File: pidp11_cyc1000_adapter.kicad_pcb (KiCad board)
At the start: 2 copper layers, 73.7 x 61 mm, 16 parts, among them J1 PIDP11_HDR, J2 USB_B_Micro, J3 PMODNIC100, J4 Conn_01x02, U1 CYC1000, U2 CP2102

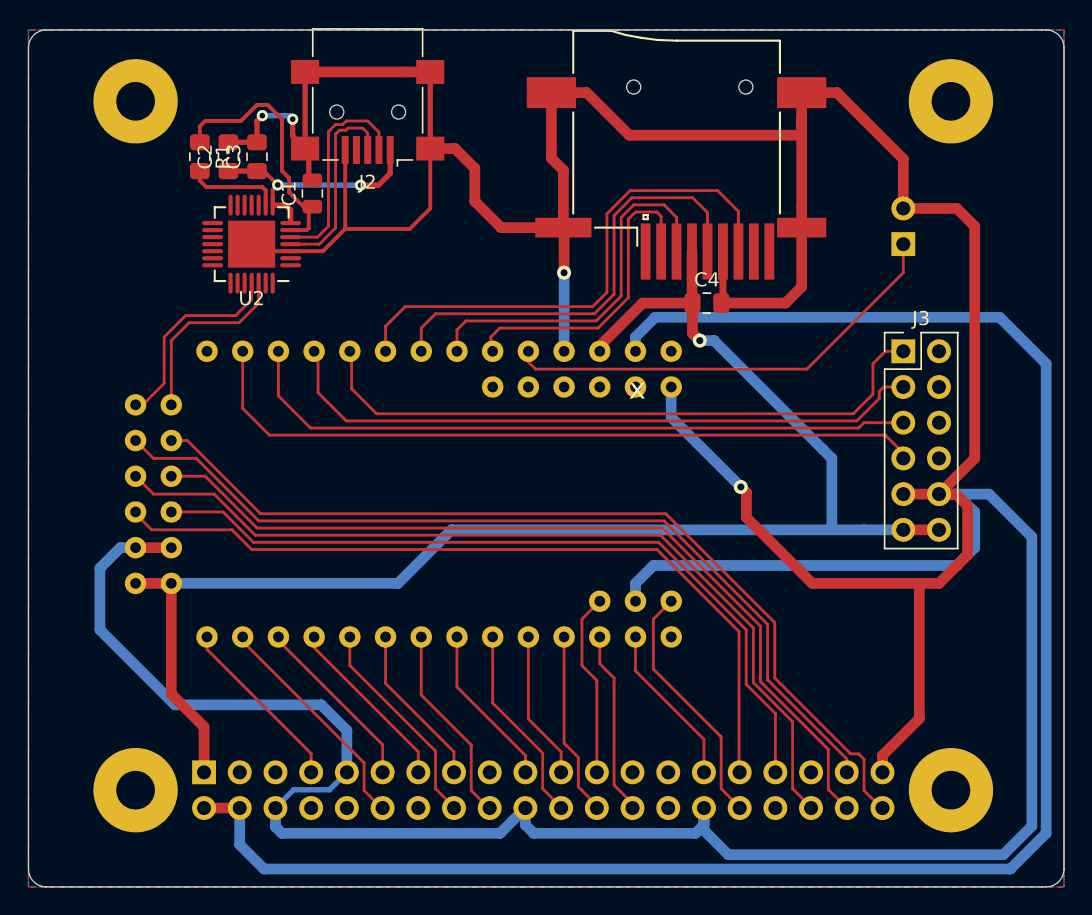
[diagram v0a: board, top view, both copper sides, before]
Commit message: add some via stitching
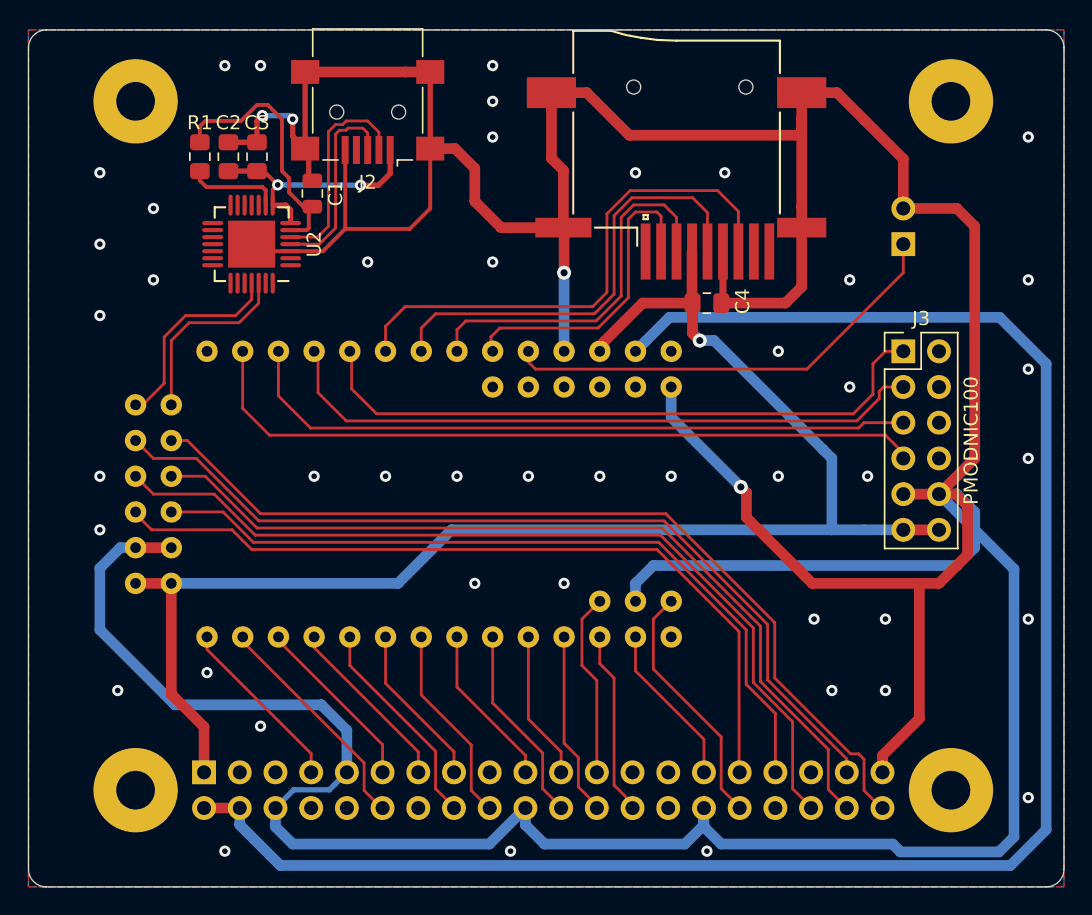
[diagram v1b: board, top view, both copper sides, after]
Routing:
- net GND: track 388.3 -> 385.9 mm, vias 4 -> 49
- net +5V: track 129.8 -> 128.1 mm
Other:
- board text added: "PMODNIC100"

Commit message: final tweaks before first test run
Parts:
- added J5: HDR_BUTT1, Connector_PinHeader_2.54mm:PinHeader_1x02_P2.54mm_Horizontal, B.Cu at (179.1, 99.1)
- added R2: 12K, Resistor_SMD:R_0805_2012Metric_Pad1.15x1.40mm_HandSolder, F.Cu at (138.6, 95.1)
- J4: value Conn_01x02 -> HDR_RESET
- moved J3 5.08 mm to (179.1, 104.1)
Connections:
- U1 pad 15: Net-(U1-Pad15) -> /ETH_SCLK
- U1 pad 16: /ETH_SCLK -> /ETH_MISO
- U1 pad 17: /ETH_MISO -> /ETH_MOSI
- U1 pad 18: /ETH_MOSI -> /ETH_CS
- U1 pad 19: /ETH_CS -> /BUTT1
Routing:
- net /BUTT1: track 0.00 -> 46.5 mm
- net GND: track 385.9 -> 343.5 mm, vias 49 -> 44
- net +3V3: track 105.9 -> 141.3 mm
- net /ETH_SCLK: track 52.8 -> 56.7 mm
- net /ETH_MISO: track 48.7 -> 51.9 mm
- net /PANEL_XLED0: track 61.9 -> 64.3 mm
- net /PANEL_XLED1: track 65.0 -> 67.4 mm
- net /PANEL_COL0: track 63.2 -> 65.6 mm
- net /ETH_CS: track 45.8 -> 44.0 mm
- net +5V: track 128.1 -> 129.8 mm
- net /PANEL_ROW0: track 62.9 -> 64.5 mm
- net /UART_RX: track 13.3 -> 14.6 mm
- net /ETH_MOSI: track 46.9 -> 48.1 mm
- net /UART_TX: track 14.5 -> 15.3 mm
- net /PANEL_COL11: track 55.4 -> 56.3 mm
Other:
- board text added: "CYC1000"
- board text added: "PiDP11"
- board text added: "PiDP11↔CYC1000 adapter"
- board text added: "Reset"
- board text added: "User"
- board text added: "desaster'19"
